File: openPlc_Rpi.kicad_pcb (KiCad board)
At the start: 2 copper layers, 155 x 108 mm, 111 parts, among them J1 Raspberry_Pi_2_3, J10 Conn_01x04, J11 Conn_01x04, J12 Conn_01x04, J13 Conn_01x04, J14 Screw_Terminal_01x10, J2 Screw_Terminal_01x04, J3 Screw_Terminal_01x02, J5 Screw_Terminal_01x12, J7 Screw_Terminal_01x12, J8 Screw_Terminal_01x02, J9 Screw_Terminal_01x02, K1 G5LE-1, K2 G5LE-1, K3 G5LE-1, K4 G5LE-1, K5 G5LE-1, K6 G5LE-1, K7 G5LE-1, K8 G5LE-1, Q1 BSS123, Q2 2N7002, Q3 2N7002, U1 power_LM2576, U2 LTV-847, U3 LTV-847, U4 power_L7812_smd, U5 MAX481E, U6 ADS1018IDGS, U7 AMS1117-3.3, U8 ULN2803A

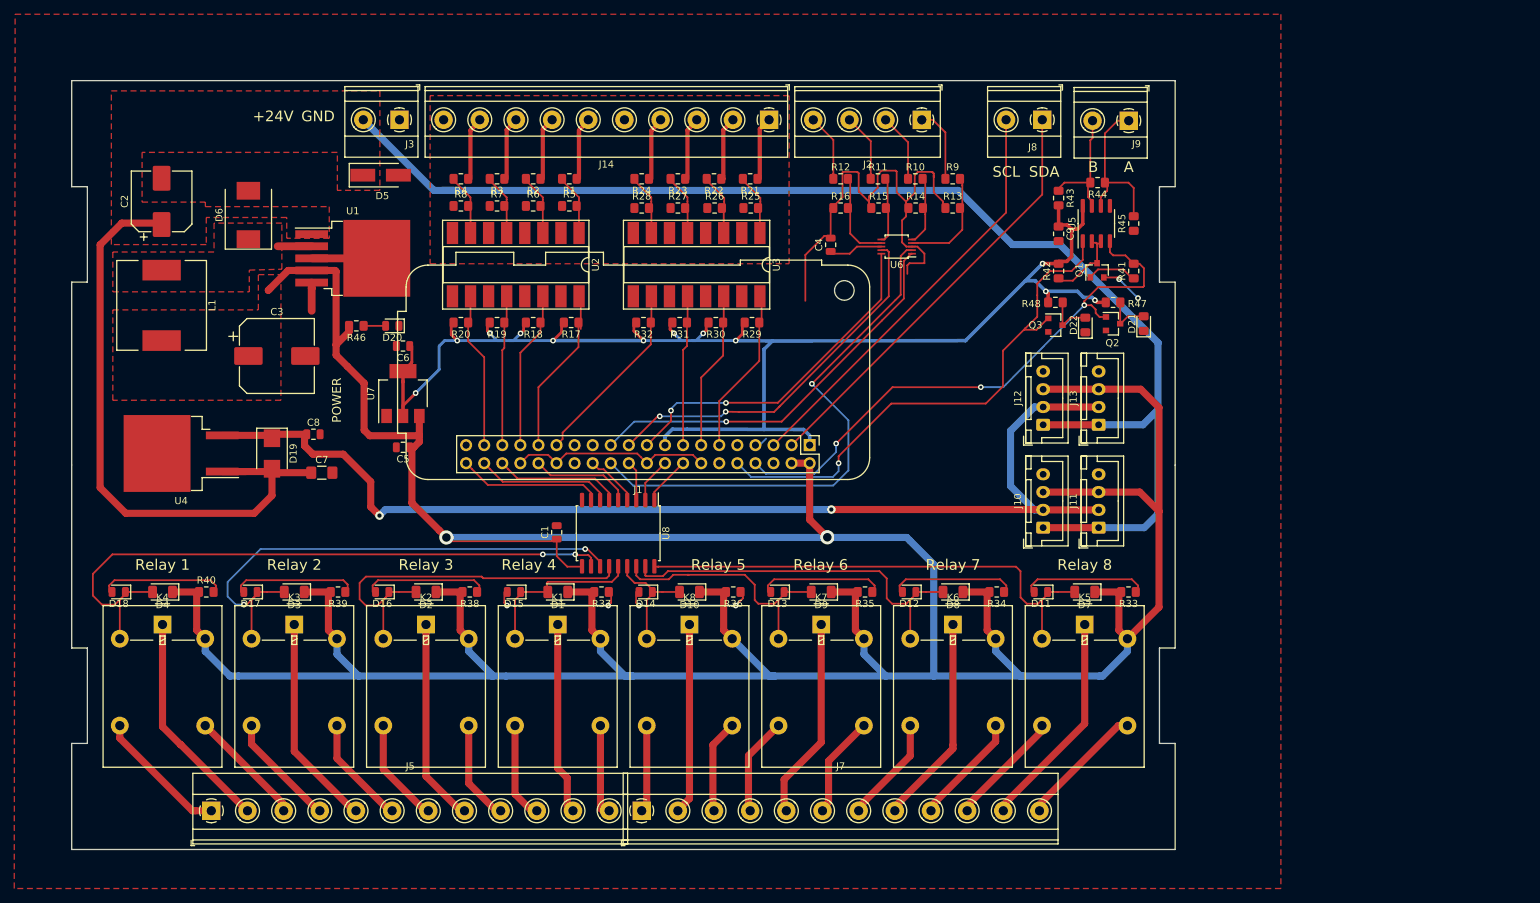
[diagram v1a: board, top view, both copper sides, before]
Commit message: [vishnu] reordered i/p resistors. Added berg strips to local library.
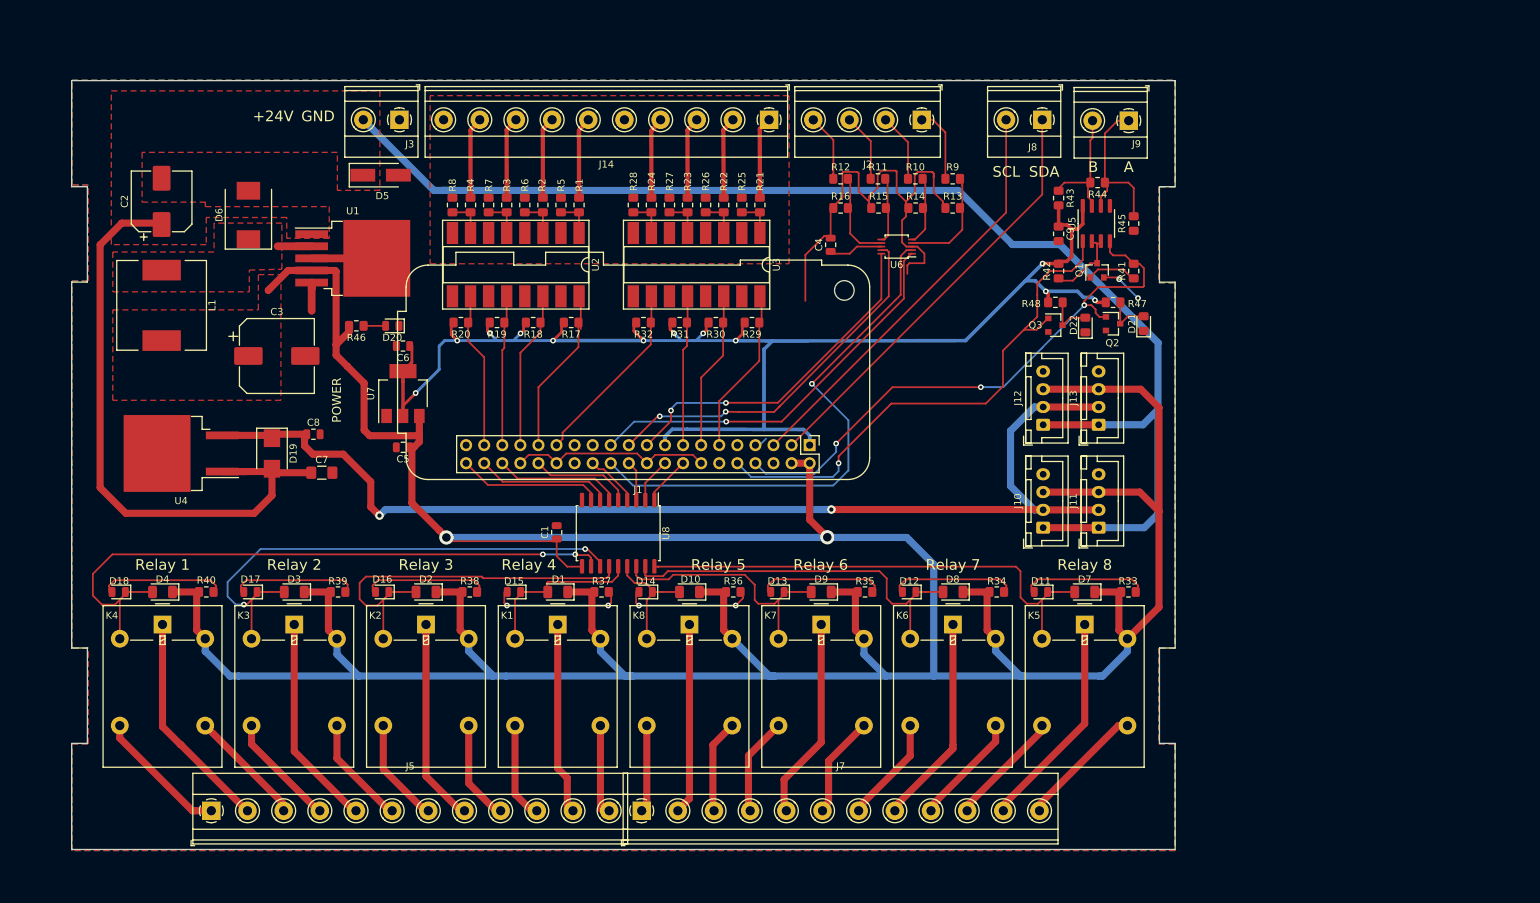
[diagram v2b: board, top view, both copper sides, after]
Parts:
- moved R21 3.92 mm to (129.9, 65.0), turned to 270 degrees
- moved R22 3.92 mm to (124.8, 65.0), turned to 270 degrees
- moved R23 3.92 mm to (119.7, 65.0), turned to 270 degrees
- moved R24 3.92 mm to (114.6, 65.0), turned to 270 degrees
- moved R1 3.92 mm to (104.5, 65.0), turned to 270 degrees
- moved R2 3.92 mm to (99.4, 65.0), turned to 270 degrees
- moved R3 3.92 mm to (94.3, 65.0), turned to 270 degrees
- moved R4 3.92 mm to (89.2, 65.0), turned to 270 degrees
- moved R25 1.33 mm to (127.3, 65.0), turned to 270 degrees
- moved R26 1.33 mm to (122.3, 65.0), turned to 270 degrees
- moved R27 1.25 mm to (117.2, 65.0), turned to 270 degrees
- moved R28 1.25 mm to (112.1, 65.0), turned to 270 degrees
- moved R5 1.19 mm to (101.9, 65.0), turned to 270 degrees
- moved R6 1.19 mm to (96.9, 65.0), turned to 270 degrees
- moved R7 1.19 mm to (91.8, 65.0), turned to 270 degrees
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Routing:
- net Net-(R21-Pad2): track 9.49 -> 5.45 mm
- net Net-(R22-Pad2): track 9.49 -> 5.45 mm
- net Net-(R24-Pad2): track 9.43 -> 5.45 mm
- net Net-(R23-Pad2): track 9.43 -> 5.45 mm
- net Net-(R4-Pad2): track 9.43 -> 5.45 mm
- net Net-(R2-Pad2): track 9.43 -> 5.47 mm
- net Net-(R1-Pad2): track 9.43 -> 5.47 mm
- net Net-(R3-Pad2): track 9.43 -> 5.47 mm
- net Net-(J14-Pad4): track 8.94 -> 11.6 mm
- net Net-(J14-Pad3): track 8.90 -> 11.6 mm
- net Net-(J14-Pad1): track 8.84 -> 11.5 mm
- net Net-(J14-Pad6): track 9.59 -> 12.2 mm
- net Net-(J14-Pad9): track 8.91 -> 11.6 mm
- net Net-(J14-Pad8): track 8.88 -> 11.5 mm
- net Net-(J14-Pad7): track 8.85 -> 11.5 mm
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- added copper zone on B.Cu, net (none)

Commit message: [vishnu] added rpi 3d step models. moved opto and added the headers. updated the netlist.
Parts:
- added J15: bergStrip_01x06_Male, fossee_openplc:bergStrip_male_1x06_P2.54mm_Vertical, F.Cu at (231.2, 90.2)
- added J16: bergStrip_01x06_Male, fossee_openplc:bergStrip_male_1x06_P2.54mm_Vertical, F.Cu at (235.8, 90.2)
- added J4: bergStrip_01x06_Male, fossee_openplc:bergStrip_male_1x06_P2.54mm_Vertical, F.Cu at (101.9, 63.1)
- added J6: bergStrip_01x06_Male, fossee_openplc:bergStrip_male_1x06_P2.54mm_Vertical, F.Cu at (127.3, 63.1)
- moved R1 4.32 mm to (104.5, 69.3)
- moved R17 4.32 mm to (103.4, 85.9)
- moved R18 4.32 mm to (98.0, 85.9)
- moved R19 4.32 mm to (93.0, 85.9)
- moved R2 4.32 mm to (99.4, 69.3)
- moved R20 4.32 mm to (87.9, 85.9)
- moved R21 4.32 mm to (129.9, 69.3)
- moved R22 4.32 mm to (124.8, 69.3)
- moved R23 4.32 mm to (119.7, 69.3)
- moved R24 4.32 mm to (114.6, 69.3)
- moved R25 4.32 mm to (127.3, 69.3)
- moved R26 4.32 mm to (122.3, 69.3)
- moved R27 4.32 mm to (117.2, 69.3)
- moved R28 4.32 mm to (112.1, 69.3)
- moved R29 4.32 mm to (128.8, 85.9)
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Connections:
- net Net-(J14-Pad1) renamed in_1
- net Net-(J14-Pad2) renamed in_2
- net Net-(J14-Pad3) renamed in_3
- net Net-(J14-Pad4) renamed in_4
- net Net-(J14-Pad6) renamed in_5
- net Net-(J14-Pad7) renamed in_6
- net Net-(J14-Pad8) renamed in_7
- net Net-(J14-Pad9) renamed in_8
- J1 pad 12: Net-(J1-Pad12) -> (no net)
- J1 pad 27: Net-(J1-Pad27) -> (no net)
- J1 pad 28: Net-(J1-Pad28) -> (no net)
- J1 pad 7: Net-(J1-Pad7) -> (no net)
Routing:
- net +3V3: track 206.9 -> 172.9 mm, vias 12 -> 5
- net GND: track 118.5 -> 132.9 mm
- net in_8: track 11.6 -> 20.6 mm
- net in_4: track 11.6 -> 18.9 mm
- net in_1: track 11.5 -> 18.2 mm
- net in_5: track 12.2 -> 18.4 mm
- net in_7: track 11.5 -> 17.2 mm
- net in_3: track 11.6 -> 16.8 mm
- net DI_3: track 24.9 -> 19.7 mm
- net +24V: track 273.6 -> 278.4 mm
- net DI_5: track 21.5 -> 17.2 mm
- net DI_6: track 22.6 -> 18.3 mm
- net DI_2: track 22.7 -> 18.4 mm
- net DI_1: track 21.7 -> 17.3 mm
- net DI_0: track 22.5 -> 18.2 mm
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- added copper zone on B.Cu, net +24V
- added copper zone on B.Cu, net /DIGND
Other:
- net class j14 - inputs added: clearance 0.4, trace_width 0.6, via_dia 0.8, via_drill 0.4
- net class j2&j6 - inputs removed

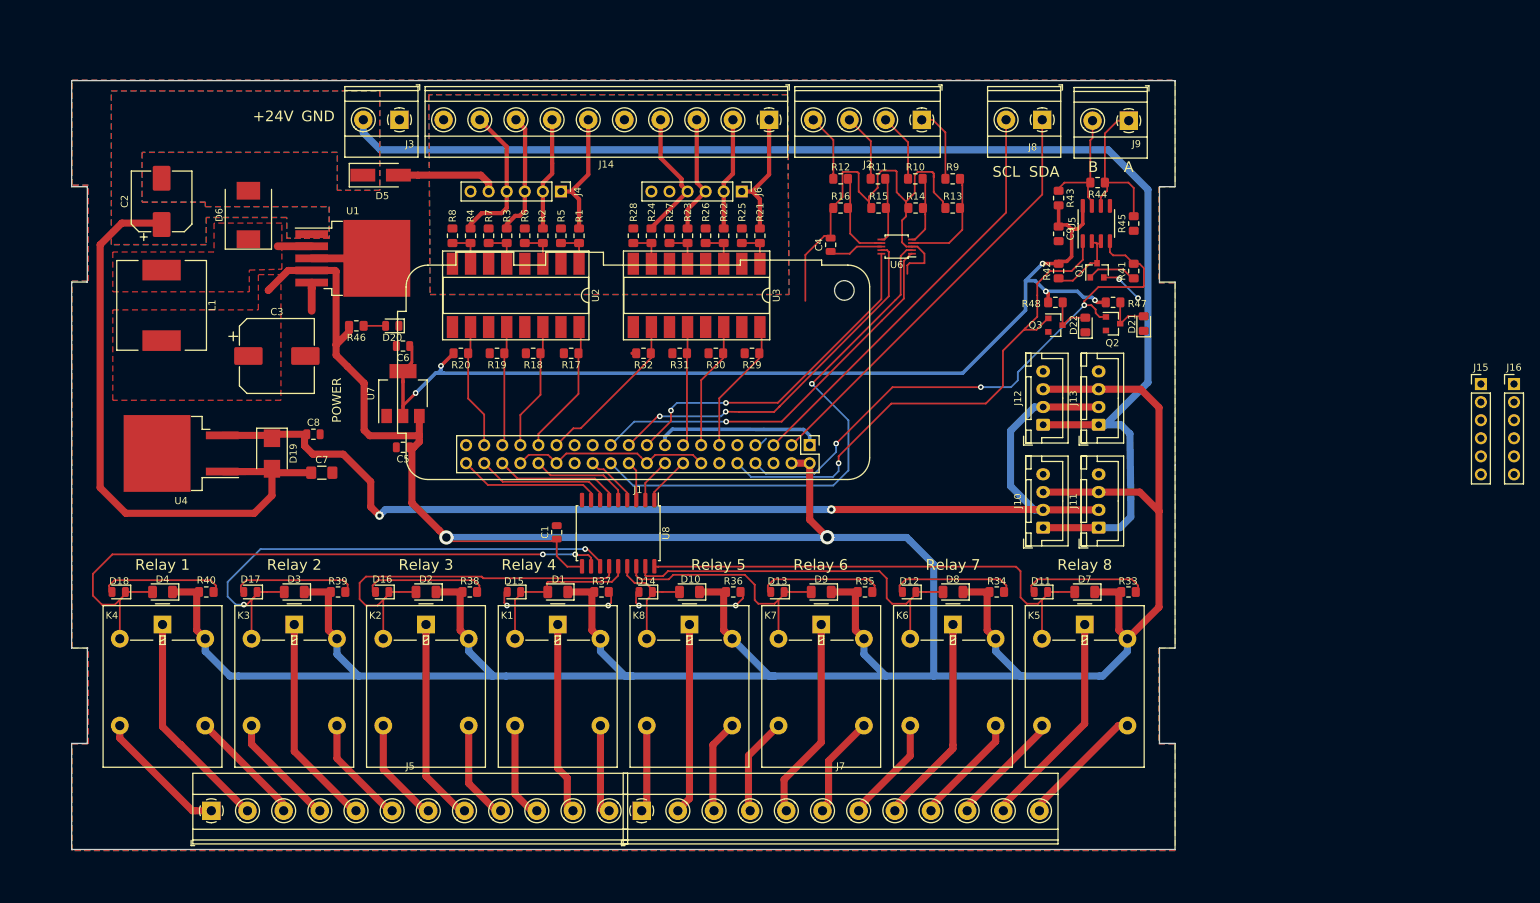
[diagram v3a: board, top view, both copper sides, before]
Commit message: [vishnu] Added male headers at input and output. PCB updated. Labels updated.
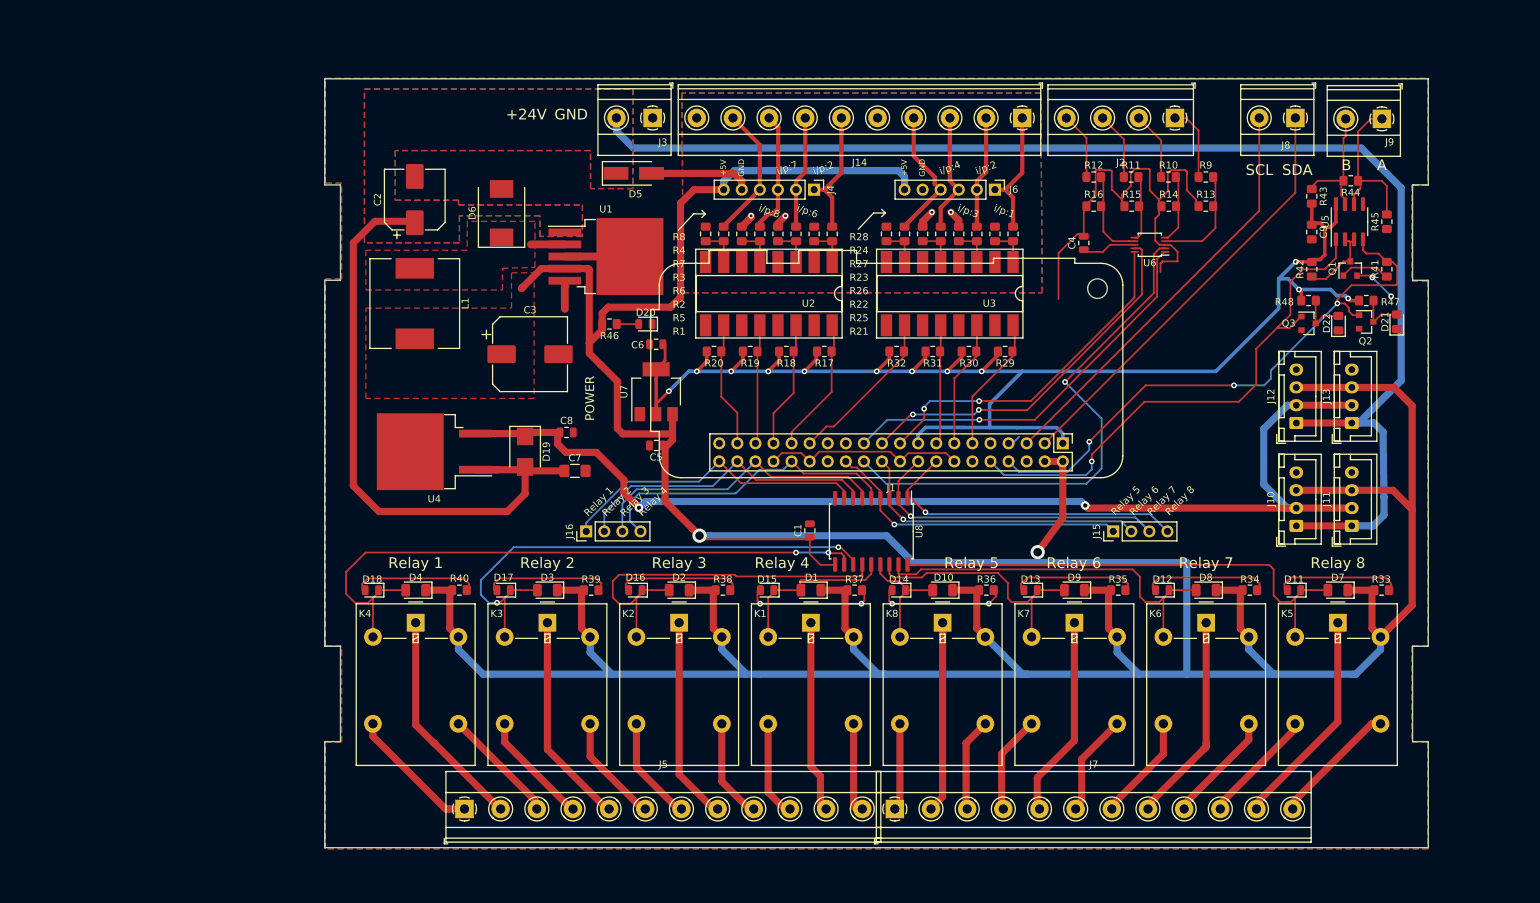
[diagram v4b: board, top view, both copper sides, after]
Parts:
- J15, J16: value bergStrip_01x06_Male -> bergStrip_01x04_Male; footprint fossee_openplc:bergStrip_male_1x06_P2.54mm_Vertical -> fossee_openplc:bergStrip_1x04_P2.54mm_Vertical
- moved J16 132.0 mm to (105.5, 110.9), turned to 90 degrees
- moved J15 55.6 mm to (179.5, 110.9), turned to 90 degrees
- moved D10 35.6 mm to (155.6, 119.1)
- moved J4 35.6 mm to (137.5, 62.9)
- moved K8 35.6 mm to (155.6, 123.7)
- moved R18 35.6 mm to (133.6, 85.6)
- moved R23 35.6 mm to (155.3, 69.1)
- moved R30 35.6 mm to (159.3, 85.6)
- moved R32 35.6 mm to (149.1, 85.6)
- moved R5 35.6 mm to (137.5, 69.1)
- moved D4 35.6 mm to (81.5, 119.1)
- moved K4 35.6 mm to (81.5, 123.7)
- moved C1 35.6 mm to (136.9, 110.7)
- moved C3 35.6 mm to (97.6, 86.0)
- moved C4 35.6 mm to (175.4, 70.4)
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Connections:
- J15 pad 1: (no net) -> DO_4
- J15 pad 2: (no net) -> DO_5
- J15 pad 3: (no net) -> DO_6
- J15 pad 4: (no net) -> DO_7
- J16 pad 1: (no net) -> DO_0
- J16 pad 2: (no net) -> DO_1
- J16 pad 3: (no net) -> DO_2
- J16 pad 4: (no net) -> DO_3
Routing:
- net +5V: track 519.1 -> 584.5 mm
- net DO_6: track 6.33 -> 46.4 mm, vias 0 -> 1
- net DO_7: track 6.85 -> 45.3 mm, vias 0 -> 1
- net DO_5: track 5.61 -> 42.1 mm, vias 0 -> 1
- net DO_4: track 7.60 -> 43.2 mm, vias 0 -> 1
- net +3V3: track 172.9 -> 206.6 mm, vias 5 -> 12
- net DO_3: track 14.2 -> 43.9 mm
- net DO_2: track 17.8 -> 42.8 mm
- net DO_1: track 19.0 -> 43.3 mm
- net DO_0: track 20.3 -> 43.8 mm
- net /DIGND: track 0.00 -> 9.05 mm, vias 0 -> 4
- net in_8: track 20.6 -> 18.9 mm
- net +12V: track 158.8 -> 157.8 mm
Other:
- board text added: "+5V"
- board text added: "i/p:1"
- board text added: "i/p:2"
- board text added: "i/p:3"
- board text added: "i/p:4"
- board text added: "i/p:6"
- board text added: "i/p:7"
- board text added: "i/p:8"
